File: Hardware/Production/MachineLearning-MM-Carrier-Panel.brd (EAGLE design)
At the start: 145 x 123.4 mm, 493 parts, among them J11 microSD, J15 CAMERA-HIMAX, J16 QWIIC_RIGHT_ANGLE, J17 USB-A, J18 JTAG, J19 MICROMOD-2222-C, J2 JTAG, J23 microSD, J28 CAMERA-HIMAX, J29 QWIIC_RIGHT_ANGLE, J3 QWIIC_RIGHT_ANGLE, J30 USB-A, J31 JTAG, J32 MICROMOD-2222-C, J36 microSD, J4 USB-A, J41 CAMERA-HIMAX, J42 QWIIC_RIGHT_ANGLE, J43 USB-A, J44 JTAG, J45 MICROMOD-2222-C, J49 microSD, J7 CAMERA-HIMAX, J9 MICROMOD-2222-C, U1 AP7361C-33FGE, U10 AP7361C-33FGE, U11 LIS2DH12, U12 AP2127K-1.8V, U2 LIS2DH12, U3 AP2127K-1.8V, U4 LIS2DH12, U5 AP7361C-33FGE, U6 AP2127K-1.8V, U7 AP7361C-33FGE, U8 LIS2DH12, U9 AP2127K-1.8V

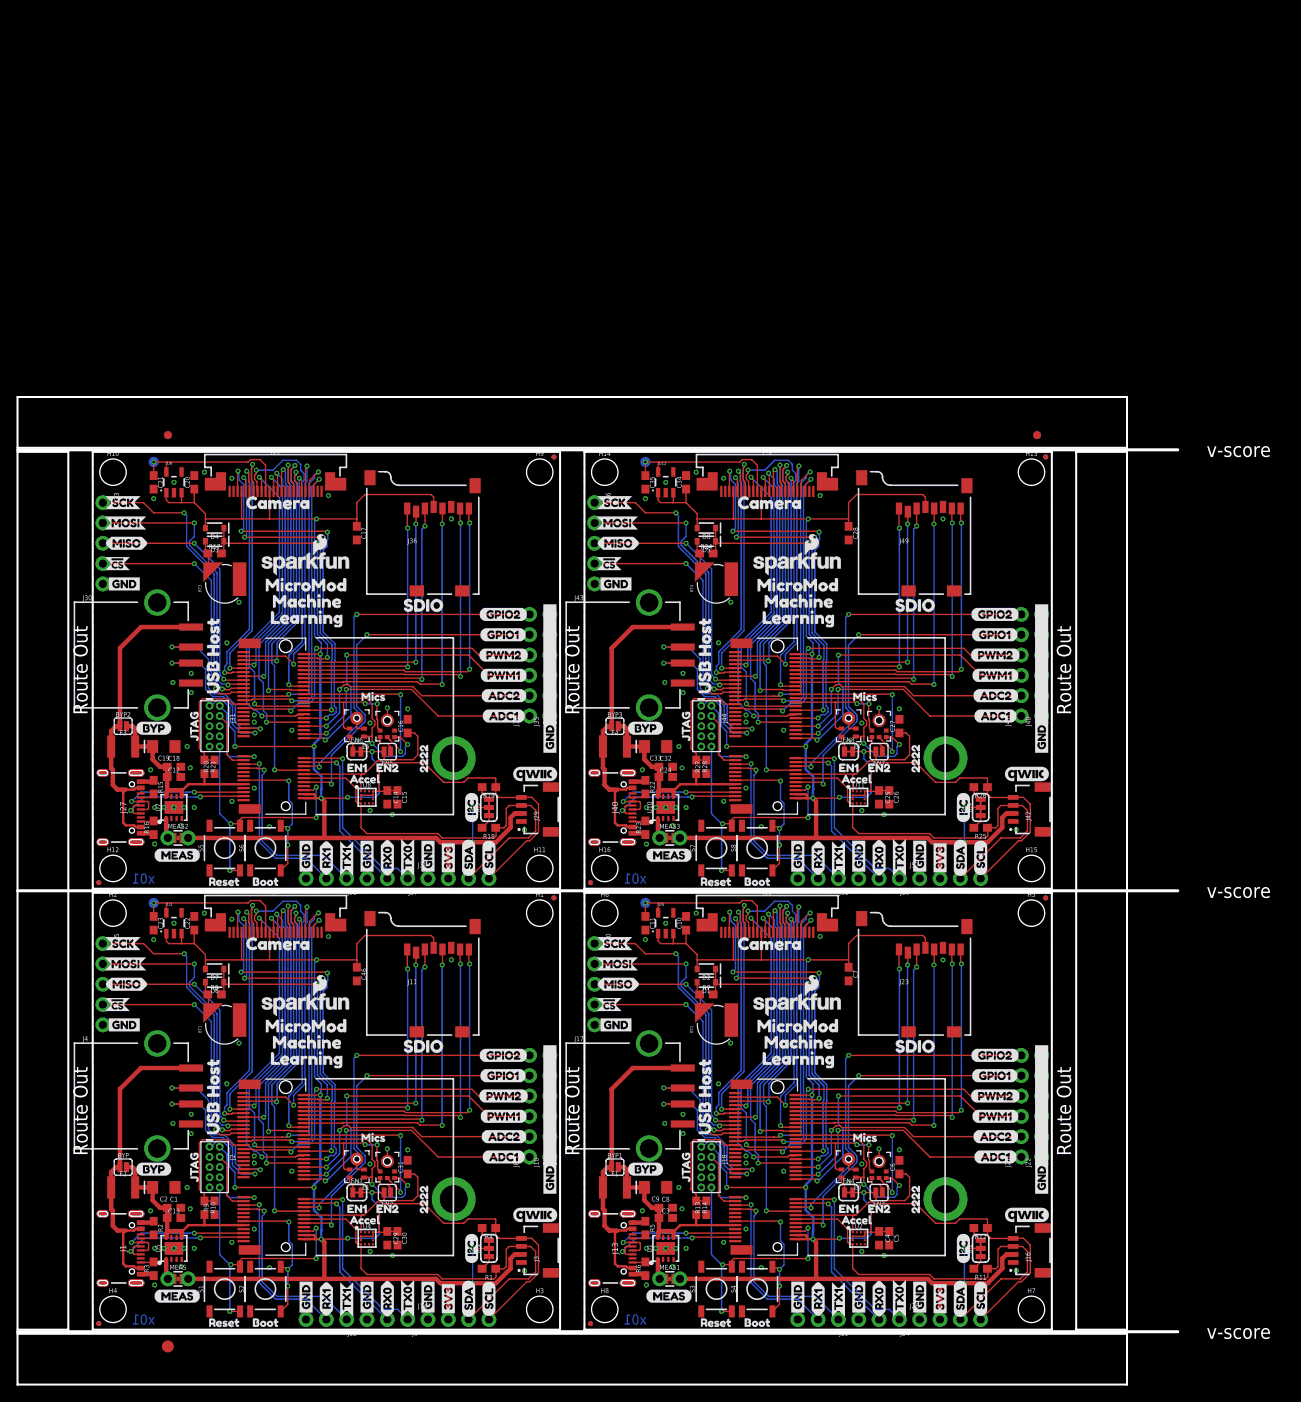
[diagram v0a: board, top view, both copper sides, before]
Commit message: Re-route camera connector for face up. Convert buzzard labels. Add power control to camera regulator.
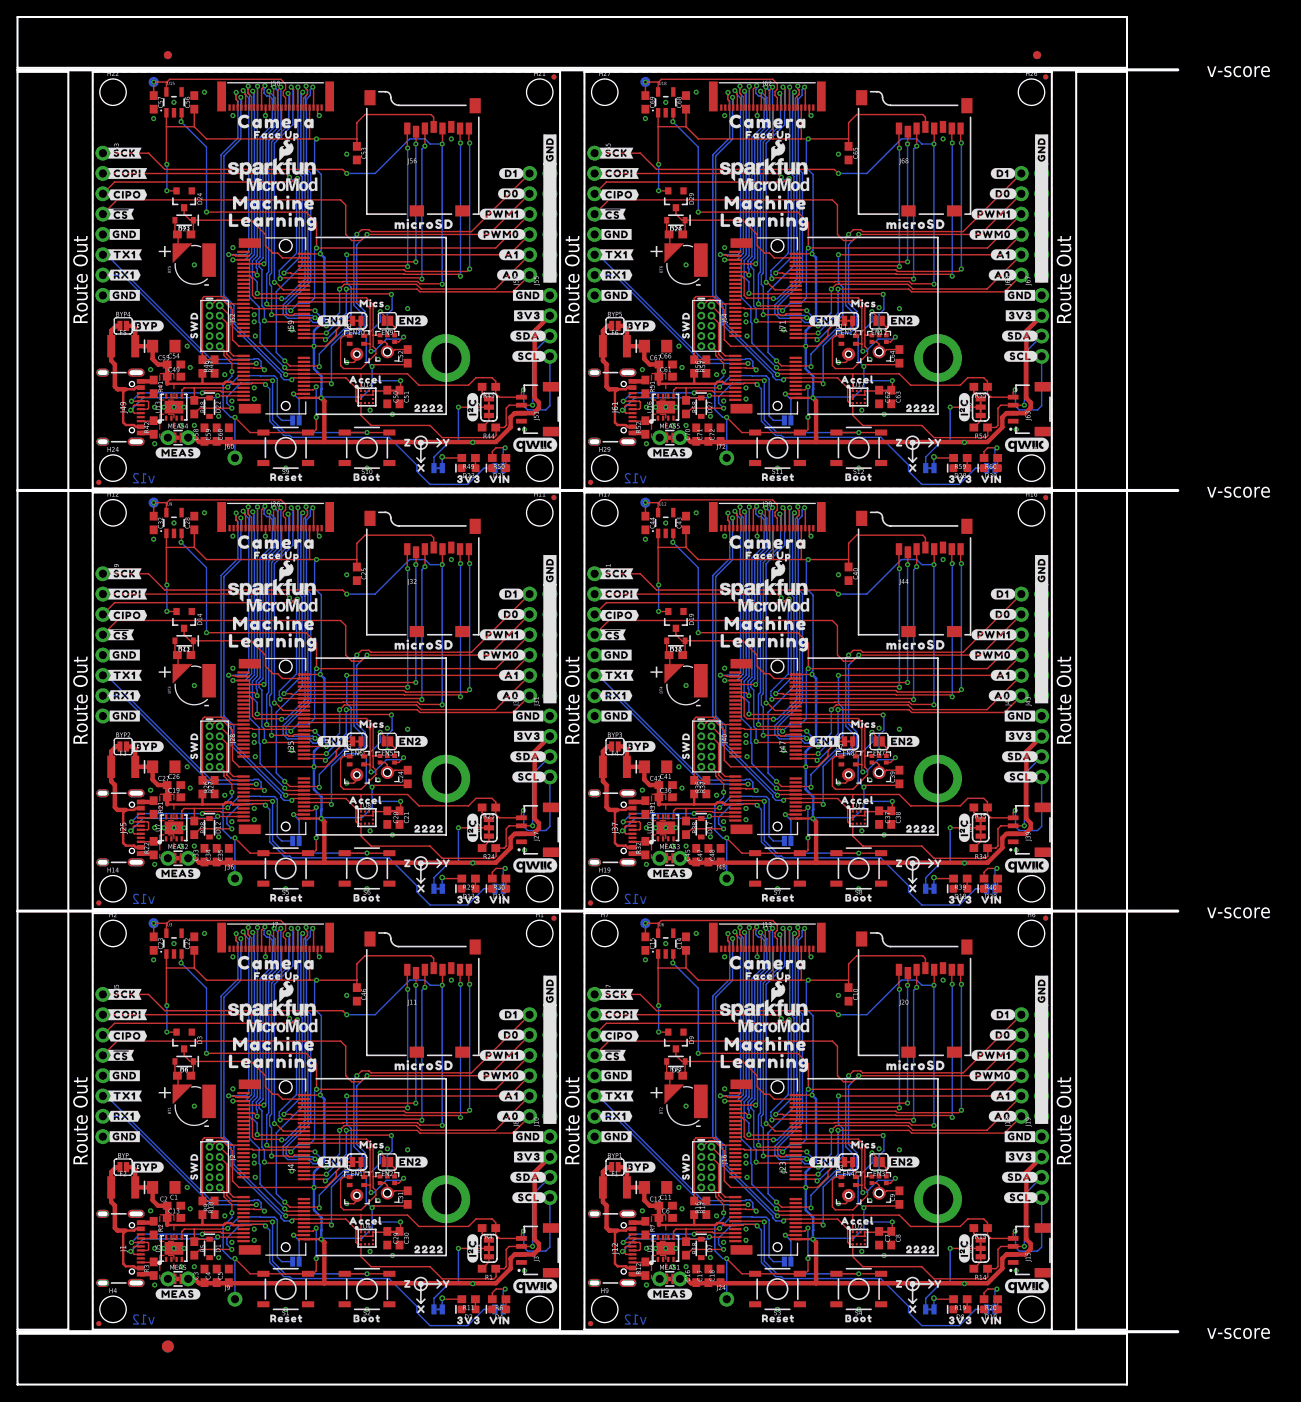
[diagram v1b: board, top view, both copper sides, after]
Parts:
- added 3V3_LED, 3V3_LED1, 3V3_LED2, 3V3_LED3, 3V3_LED4, 3V3_LED5, EN10, EN12, VIN_LED, VIN_LED1, VIN_LED2, VIN_LED3, VIN_LED4, VIN_LED5: (no value), SparkFun-Jumpers:SMT-JUMPER_2_NC_TRACE_SILK
- added BT5, BT6: ML414H, SparkFun-Batteries:ML414H_IV01E
- added BYP4, BYP5: JUMPER-SMT_2_NO_SILK, SparkFun-Jumpers:SMT-JUMPER_2_NO_SILK
- added C36, C48, C49, C60, C61, C72: 0.22uF, SparkFun-Capacitors:0603
- added C37, C43, C45, C50, C56, C58, C62, C68, C70: 1.0uF, SparkFun-Capacitors:0603
- added C38, C39, C40, C41, C44, C47, C51, C52, C53, C54, C57, C59, C63, C64, C65, C66, C69, C71: 0.1uF, SparkFun-Capacitors:0603
- added C42, C55, C67: 10uF, SparkFun-Capacitors:EIA3216
- added D10, D15, D20, D25, D30: Yellow, SparkFun-LED:LED-0603
- added D11, D16, D21, D26: 3A/10V/280mV, SparkFun-DiscreteSemi:SOD-323
- added D12, D17, D22, D27: 3.3V, SparkFun-DiscreteSemi:SOD-323
- added D13, D18, D23, D28: RED, SparkFun-LED:LED-0603
- added D14, D19, D24, D29, D9: BAS70-05, SparkFun-DiscreteSemi:SOT23-3
- added E$6: (no value), SparkFun-Retired:FIDUCIAL-1.5X3
- added E10, E12: ICS-43434, Teensy:ICS-43434
- added E11, E9: SPH0641LM4H-1, SparkFun-Sensors:SPH0641LM4H-1_MICROPHONE
- added EN11, EN9, VE, VE1, VE2, VE3, VE4, VE5: (no value), SparkFun-Jumpers:SMT-JUMPER_2_NO_SILK
- added F5, F6: 6V/2A, SparkFun-Fuses:1210
- added FD17, FD18, FD19, FD20, FD21, FD22, FD23, FD24: FIDUCIALUFIDUCIAL, SparkFun-Aesthetics:FIDUCIAL-MICRO
- added H17, H18, H19, H21, H22, H23, H24, H26, H27, H28, H29: STAND-OFF, SparkFun-Hardware:STAND-OFF
- added H20, H25, H30: STAND-OFF-REFLOW2.5MM_TALL, SparkFun-Hardware:STAND-OFF-REFLOW-M2.5
- added J53, J65: SPI, SparkFun-Connectors:1X05_NO_SILK
- added J54, J66: Dedicated, SparkFun-Connectors:1X06_NO_SILK
- added J55, J67: (no value), SparkFun-Connectors:1X06_NO_SILK
- added J56, J68: microSD, SparkFun-Connectors:MICRO-SD-SOCKET
- added J57, J69: UART, SparkFun-Connectors:1X03_NO_SILK
- added J58, J70: (no value), SparkFun-Connectors:1X04_NO_SILK
- added J59, J71: MICROMOD-2222-C, SparkFun-MicroMod:M.2-CONNECTOR-E
- added J60, J72: (no value), SparkFun-Connectors:1X01_NO_SILK
- added J61: (no value), SparkFun-Connectors:USB-C-16P-2LAYER-PADS
- added J62: CAMERA-HIMAXFACEUP, SparkFun-Connectors:FPC05024-42201
- added J63: QWIIC_RIGHT_ANGLE, SparkFun-Connectors:JST04_1MM_RA
- added J64: JTAG, SparkFun-Connectors:2X5-PTH-1.27MM
- added JP5, JP6: (no value), SparkFun-Jumpers:SMT-JUMPER_3_2-NC_TRACE_SILK
- added LOGO17, LOGO20, LOGO21, LOGO24: SFE_LOGO_NAME_FLAME.1_INCH, SparkFun-Aesthetics:SFE_LOGO_NAME_FLAME_.1
- added LOGO18, LOGO22: QWIIC_LOGO_CONNECTOR, SparkFun-Aesthetics:QWIIC_5.5MM
- added LOGO19, LOGO23: OSHW-LOGOMINI, SparkFun-Aesthetics:OSHW-LOGO-MINI
- added MEAS4, MEAS5: (no value), SparkFun-Jumpers:COMBO-JUMPER_2_NC_TRACE
- added R29, R39, R49, R59: 1k, SparkFun-Resistors:0603
- added R30, R40, R50, R60: 4.7k, SparkFun-Resistors:0603
- added R31, R32, R41, R42, R51, R52: 5.1k, SparkFun-Resistors:0603
- added R33, R43, R53: 3.3k, SparkFun-Resistors:0603
- added R34, R35, R44, R45, R54, R55: 2.2k, SparkFun-Resistors:0603
- added R36, R46, R56: 10k, SparkFun-Resistors:0603
- added R37, R47, R57: 20k, SparkFun-Resistors:0603
- added R38, R48, R58: 100k, SparkFun-Resistors:0603
- added S10, S12: BOOT, SparkFun-Switches:TACTILE_SWITCH_SMD_5.2MM
- added S11, S9: Reset, SparkFun-Switches:TACTILE_SWITCH_SMD_5.2MM
- added TP4, TP5: TEST-POINT3X5, SparkFun-Connectors:PAD.03X.05
- added U$257, U$324, U$391: (no value), output:#RST#1
- added U$258, U$325, U$392: (no value), output:#VE#0
- added U$259, U$326, U$393: (no value), output:#I�C#0
- added U$260, U$268, U$327, U$335, U$394, U$402: (no value), output:MACHINE0
- added U$261, U$267, U$328, U$334, U$395, U$401: (no value), output:LEARNING1
- added U$262, U$329, U$396: (no value), output:CAMERA0
- added U$263, U$330, U$397: (no value), output:FACE_UP0
- added U$264, U$331, U$398: (no value), output:#3V3#0
- added U$265, U$332, U$399: (no value), output:#VIN#1
- added U$266, U$333, U$400: (no value), output:MICROSD0
- added U$269, U$270, U$336, U$337: (no value), SparkFun-MicroMod:MICROMOD_LOGO_.35
- added U$271, U$272, U$338, U$339: (no value), output:##CS##3
- added U$273, U$274, U$340, U$341: (no value), output:#CIPO#2
- added U$275, U$276, U$342, U$343: (no value), output:#COPI#1
- added U$277, U$278, U$285, U$286, U$344, U$345, U$352, U$353: (no value), output:#GND#4
- added U$279, U$280, U$346, U$347: (no value), output:#RX1#6
- added U$281, U$282, U$348, U$349: (no value), output:#SCK#0
- added U$283, U$284, U$350, U$351: (no value), output:#TX1#5
- added U$287, U$288, U$354, U$355: (no value), output:#A0#5
- added U$289, U$290, U$356, U$357: (no value), output:#A1#4
- added U$291, U$292, U$358, U$359: (no value), output:#D0#1
- added U$293, U$294, U$360, U$361: (no value), output:#D1#0
- added U$295, U$296, U$362, U$363: (no value), output:#PWM0#3
- added U$297, U$298, U$364, U$365: (no value), output:#PWM1#2
- added U$299, U$300, U$303, U$304, U$366, U$367, U$370, U$371: (no value), output:#GND#0
- added U$301, U$302, U$368, U$369: (no value), output:#3V3#1
- added U$305, U$306, U$372, U$373: (no value), output:#SCL#3
- added U$307, U$308, U$374, U$375: (no value), output:#SDA#2
- added U$309, U$376: (no value), output:3V37
- added U$310, U$377: (no value), output:22223
- added U$311, U$378: (no value), output:ACCEL4
- added U$312, U$379: (no value), output:BOOT5
- added U$313, U$380: (no value), output:RESET6
- added U$314, U$381: (no value), output:VIN8
- added U$315, U$382: (no value), output:X1
- added U$316, U$383: (no value), output:Y2
- added U$317, U$384: (no value), output:Z0
- added U$318, U$385: (no value), output:#EN1#3
- added U$319, U$386: (no value), output:#EN2#4
- added U$320, U$387: (no value), output:#MEAS#2
- added U$321, U$388: (no value), output:SWD0
- added U$322, U$389: (no value), output:#BYP#1
- added U$323, U$390: (no value), output:MICS0
- added U13, U16: AP7361C-33FGE, SparkFun-IC-Power:UDFN-8
- added U14, U17: LIS2DH12, SparkFun-Sensors:LGA-12-LISDH12
- added U15, U18: AP2127K-1.8V, SparkFun-IC-Power:SOT23-5
- C10, C25, C34, C4: value 1.0uF -> 0.1uF
- C12: value 0.22uF -> 10uF; device SparkFun-Capacitors:0603 -> SparkFun-Capacitors:EIA3216
- C16, C28, C7: value 0.1uF -> 1.0uF
- C18, C35, C5, C6: value 0.1uF -> 0.22uF
- C19: value 10uF -> 0.22uF; device SparkFun-Capacitors:EIA3216 -> SparkFun-Capacitors:0603
- C24: value 0.22uF -> 0.1uF
- C27: value 0.1uF -> 10uF; device SparkFun-Capacitors:0603 -> SparkFun-Capacitors:EIA3216
- C3: value 0.22uF -> 1.0uF
- C33: value 10uF -> 1.0uF; device SparkFun-Capacitors:EIA3216 -> SparkFun-Capacitors:0603
- C9: value 10uF -> 0.1uF; device SparkFun-Capacitors:EIA3216 -> SparkFun-Capacitors:0603
- D1: value 3A/10V/280mV -> 3.3V
- D2, D8: value 1A/23V/620mV -> RED; device SparkFun-DiscreteSemi:SOD-323 -> SparkFun-LED:LED-0603
- D3: value 3A/10V/280mV -> BAS70-05; device SparkFun-DiscreteSemi:SOD-323 -> SparkFun-DiscreteSemi:SOT23-3
- D4: value 1A/23V/620mV -> Yellow; device SparkFun-DiscreteSemi:SOD-323 -> SparkFun-LED:LED-0603
- D7: value 1A/23V/620mV -> 3.3V
- F1, F2, F3, F4: value 2A/5V -> 6V/2A
- H10, H15, H5: value STAND-OFF -> STAND-OFF-REFLOW2.5MM_TALL; device SparkFun-Hardware:STAND-OFF -> SparkFun-Hardware:STAND-OFF-REFLOW-M2.5
- J1: device SparkFun-Connectors:USB-C-16P -> SparkFun-Connectors:USB-C-16P-2LAYER-PADS
- J12, J25, J37: device SparkFun-Connectors:1X03_NO_SILK -> SparkFun-Connectors:USB-C-16P-2LAYER-PADS
- J13: value (none) -> CAMERA-HIMAXFACEUP; device SparkFun-Connectors:USB-C-16P -> SparkFun-Connectors:FPC05024-42201
- J15: value CAMERA-HIMAX -> QWIIC_RIGHT_ANGLE; device SparkFun-Connectors:FPC-24-AMPHENOL-SFV24R-1STE1HLF -> SparkFun-Connectors:JST04_1MM_RA
- J16: value QWIIC_RIGHT_ANGLE -> JTAG; device SparkFun-Connectors:JST04_1MM_RA -> SparkFun-Connectors:2X5-PTH-1.27MM
- J17: value USB-A -> SPI; device SparkFun-Connectors:USB-A-S-SILK-FEMALE -> SparkFun-Connectors:1X05_NO_SILK
- J18: value JTAG -> Dedicated; device SparkFun-Connectors:2X5-PTH-1.27MM -> SparkFun-Connectors:1X06_NO_SILK
- J19: value MICROMOD-2222-C -> (none); device Teensy:M.2-CONNECTOR-E -> SparkFun-Connectors:1X06_NO_SILK
- J20: value (none) -> microSD; device SparkFun-Connectors:1X05_NO_SILK -> SparkFun-Connectors:MICRO-SD-SOCKET
- J21: value (none) -> UART; device SparkFun-Connectors:1X06_NO_SILK -> SparkFun-Connectors:1X03_NO_SILK
- J22, J34: device SparkFun-Connectors:1X06_NO_SILK -> SparkFun-Connectors:1X04_NO_SILK
- J23: value microSD -> MICROMOD-2222-C; device SparkFun-Connectors:MICRO-SD-SOCKET -> SparkFun-MicroMod:M.2-CONNECTOR-E
- J24: device SparkFun-Connectors:1X03_NO_SILK -> SparkFun-Connectors:1X01_NO_SILK
- J26: value (none) -> CAMERA-HIMAXFACEUP; device SparkFun-Connectors:1X04_NO_SILK -> SparkFun-Connectors:FPC05024-42201
- J27: value (none) -> QWIIC_RIGHT_ANGLE; device SparkFun-Connectors:USB-C-16P -> SparkFun-Connectors:JST04_1MM_RA
- J28: value CAMERA-HIMAX -> JTAG; device SparkFun-Connectors:FPC-24-AMPHENOL-SFV24R-1STE1HLF -> SparkFun-Connectors:2X5-PTH-1.27MM
- J29: value QWIIC_RIGHT_ANGLE -> SPI; device SparkFun-Connectors:JST04_1MM_RA -> SparkFun-Connectors:1X05_NO_SILK
- J30: value USB-A -> Dedicated; device SparkFun-Connectors:USB-A-S-SILK-FEMALE -> SparkFun-Connectors:1X06_NO_SILK
- J31: value JTAG -> (none); device SparkFun-Connectors:2X5-PTH-1.27MM -> SparkFun-Connectors:1X06_NO_SILK
- J32: value MICROMOD-2222-C -> microSD; device Teensy:M.2-CONNECTOR-E -> SparkFun-Connectors:MICRO-SD-SOCKET
- J33: value (none) -> UART; device SparkFun-Connectors:1X05_NO_SILK -> SparkFun-Connectors:1X03_NO_SILK
- J35, J47: value (none) -> MICROMOD-2222-C; device SparkFun-Connectors:1X06_NO_SILK -> SparkFun-MicroMod:M.2-CONNECTOR-E
- J36: value microSD -> (none); device SparkFun-Connectors:MICRO-SD-SOCKET -> SparkFun-Connectors:1X01_NO_SILK
- J38, J50: value (none) -> CAMERA-HIMAXFACEUP; device SparkFun-Connectors:1X03_NO_SILK -> SparkFun-Connectors:FPC05024-42201
- J39: value (none) -> QWIIC_RIGHT_ANGLE; device SparkFun-Connectors:1X04_NO_SILK -> SparkFun-Connectors:JST04_1MM_RA
- J4: value USB-A -> MICROMOD-2222-C; device SparkFun-Connectors:USB-A-S-SILK-FEMALE -> SparkFun-MicroMod:M.2-CONNECTOR-E
- J40: value (none) -> JTAG; device SparkFun-Connectors:USB-C-16P -> SparkFun-Connectors:2X5-PTH-1.27MM
- J41: value CAMERA-HIMAX -> SPI; device SparkFun-Connectors:FPC-24-AMPHENOL-SFV24R-1STE1HLF -> SparkFun-Connectors:1X05_NO_SILK
- J42: value QWIIC_RIGHT_ANGLE -> Dedicated; device SparkFun-Connectors:JST04_1MM_RA -> SparkFun-Connectors:1X06_NO_SILK
- J43: value USB-A -> (none); device SparkFun-Connectors:USB-A-S-SILK-FEMALE -> SparkFun-Connectors:1X06_NO_SILK
- J44: value JTAG -> microSD; device SparkFun-Connectors:2X5-PTH-1.27MM -> SparkFun-Connectors:MICRO-SD-SOCKET
- J45: value MICROMOD-2222-C -> UART; device Teensy:M.2-CONNECTOR-E -> SparkFun-Connectors:1X03_NO_SILK
- J46: device SparkFun-Connectors:1X05_NO_SILK -> SparkFun-Connectors:1X04_NO_SILK
- J48: device SparkFun-Connectors:1X06_NO_SILK -> SparkFun-Connectors:1X01_NO_SILK
- J49: value microSD -> (none); device SparkFun-Connectors:MICRO-SD-SOCKET -> SparkFun-Connectors:USB-C-16P-2LAYER-PADS
- J5: value (none) -> SPI
- J51: value (none) -> QWIIC_RIGHT_ANGLE; device SparkFun-Connectors:1X03_NO_SILK -> SparkFun-Connectors:JST04_1MM_RA
- J52: value (none) -> JTAG; device SparkFun-Connectors:1X04_NO_SILK -> SparkFun-Connectors:2X5-PTH-1.27MM
- J6: value (none) -> UART
- J7: value CAMERA-HIMAX -> CAMERA-HIMAXFACEUP; device SparkFun-Connectors:FPC-24-AMPHENOL-SFV24R-1STE1HLF -> SparkFun-Connectors:FPC05024-42201
- J8: value (none) -> Dedicated
- J9: value MICROMOD-2222-C -> (none); device Teensy:M.2-CONNECTOR-E -> SparkFun-Connectors:1X01_NO_SILK
- R11, R19: value 2.2k -> 1k
- R12: value 2.2k -> 5.1k
- R13: value 10k -> 3.3k
- R14: value 20k -> 2.2k
- R15: value 5.1k -> 2.2k
- R16: value 5.1k -> 10k
- R17: value 1k -> 20k
- R18: value 2.2k -> 100k
- R20: value 10k -> 4.7k
- R21: value 20k -> 5.1k
- R23: value 5.1k -> 3.3k
- R24: value 1k -> 2.2k
- R26: value 2.2k -> 10k
- R27: value 10k -> 20k
- R28: value 20k -> 100k
- R5: value 5.1k -> 100k
- R6: value 5.1k -> 4.7k
- R7: value 1k -> 5.1k
- R8: value 1k -> 3.3k
- U$1: device buzzard_labels (11):ACCEL6 -> output:#EN1#3
- U$10: device SparkFun-Buzzard:!CS_O -> output:#D0#1
- U$100, U$167: device SparkFun-Buzzard:GND_P -> output:#3V3#1
- U$101: device buzzard_labels (6):RX01 -> output:#3V3#1
- U$102, U$166: device buzzard_labels (6):TX02 -> output:#GND#0
- U$103, U$11: device SparkFun-Buzzard:GND_P -> output:#GND#0
- U$104: device SparkFun-Buzzard:3V3_P -> output:#SCL#3
- U$105: device SparkFun-Buzzard:SDA_IO -> output:#SCL#3
- U$106: device SparkFun-Buzzard:SCL_IO -> output:#SDA#2
- U$107: device SparkFun-Buzzard:SCK_O -> output:#SDA#2
- U$108: device SparkFun-Buzzard:MOSI_O -> output:3V37
- U$109: device SparkFun-Buzzard:MISO_I -> output:22223
- U$110: device SparkFun-Buzzard:!CS_O -> output:ACCEL4
- U$111: device SparkFun-Buzzard:GND_P -> output:BOOT5
- U$112: device buzzard_labels (9):22229 -> output:RESET6
- U$113: device buzzard_labels (9):GPIO110 -> output:VIN8
- U$114: device buzzard_labels (9):GPIO211 -> output:X1
- U$115: device buzzard_labels (10):ADC12 -> output:Y2
- U$116: device buzzard_labels (10):ADC23 -> output:Z0
- U$117: device buzzard_labels (10):PWM10 -> output:#EN1#3
- U$118, U$185: device buzzard_labels (10):PWM21 -> output:#EN2#4
- U$119: device buzzard_labels (9):GPIO211 -> output:#MEAS#2
- U$12: device buzzard_labels (9):GPIO110 -> output:#GND#0
- U$120: device buzzard_labels (9):GPIO110 -> output:SWD0
- U$121: device buzzard_labels (10):PWM21 -> output:#BYP#1
- U$122: device buzzard_labels (10):PWM10 -> output:MICS0
- U$123, U$17: device buzzard_labels (10):ADC23 -> output:#RST#1
- U$124: device buzzard_labels (10):ADC12 -> output:#VE#0
- U$125: device buzzard_labels (11):MICROMOD0 -> output:#I�C#0
- U$126: device buzzard_labels (11):MACHINE2 -> output:MACHINE0
- U$127: device buzzard_labels (11):LEARNING3 -> output:LEARNING1
- U$128: device SparkFun-Buzzard:GND_P -> output:CAMERA0
- U$129: device buzzard_labels (9):RESET3 -> output:FACE_UP0
- U$13: device buzzard_labels (9):GPIO211 -> output:#3V3#1
- U$130: device SparkFun-Buzzard:MEAS -> output:#3V3#0
- U$131: device SparkFun-Buzzard:MOSI_O -> output:#VIN#1
- U$132: device SparkFun-Buzzard:MISO_I -> output:MICROSD0
- U$133: device SparkFun-Buzzard:SCK_O -> output:LEARNING1
- U$134: device SparkFun-Buzzard:!CS_O -> output:MACHINE0
- U$135, U$136, U$53, U$54: device SparkFun-Buzzard:GND_P -> SparkFun-MicroMod:MICROMOD_LOGO_.35
- U$137: device SparkFun-Buzzard:JTAG_TO -> output:##CS##3
- U$138: device buzzard_labels (10):BOOT2 -> output:##CS##3
- U$139: device buzzard_labels (10):USB_HOST0 -> output:#CIPO#2
- U$14: device buzzard_labels (10):PWM10 -> output:#3V3#1
- U$140: device buzzard_labels (10):SDIO1 -> output:#CIPO#2
- U$141: device buzzard_labels (11):ACCEL6 -> output:#COPI#1
- U$142: device buzzard_labels (11):CAMERA5 -> output:#COPI#1
- U$143: device buzzard_labels (11):LEARNING3 -> output:#GND#4
- U$144: device buzzard_labels (11):MACHINE2 -> output:#GND#4
- U$145, U$64: device buzzard_labels (11):MICROMOD0 -> output:#RX1#6
- U$146: device buzzard_labels (12):MICS0 -> output:#RX1#6
- U$147: device SparkFun-Buzzard:BYP -> output:#SCK#0
- U$148: device buzzard_labels (6):RX01 -> output:#SCK#0
- U$149: device buzzard_labels (6):RX10 -> output:#TX1#5
- U$15: device buzzard_labels (10):PWM21 -> output:#GND#0
- U$150: device buzzard_labels (6):TX02 -> output:#TX1#5
- U$151: device buzzard_labels (6):TX13 -> output:#GND#4
- U$152: device SparkFun-Buzzard:GND_P -> output:#GND#4
- U$153, U$221, U$6: device SparkFun-Buzzard:GND_P -> output:#A0#5
- U$154: device buzzard_labels (7):EN13 -> output:#A0#5
- U$155: device buzzard_labels (7):EN24 -> output:#A1#4
- U$156: device SparkFun-Buzzard:I2C -> output:#A1#4
- U$157, U$225: device SparkFun-Buzzard:GND_P -> output:#D0#1
- U$158: device SparkFun-Buzzard:3V3_P -> output:#D0#1
- U$159: device SparkFun-Buzzard:SDA_IO -> output:#D1#0
- U$16: device buzzard_labels (10):ADC12 -> output:#GND#0
- U$160: device SparkFun-Buzzard:SCL_IO -> output:#D1#0
- U$161, U$228, U$32: device SparkFun-Buzzard:GND_P -> output:#PWM0#3
- U$162: device buzzard_labels (6):RX10 -> output:#PWM0#3
- U$163: device buzzard_labels (6):TX13 -> output:#PWM1#2
- U$164, U$231, U$42, U$97: device SparkFun-Buzzard:GND_P -> output:#PWM1#2
- U$165: device buzzard_labels (6):RX01 -> output:#GND#0
- U$168: device SparkFun-Buzzard:3V3_P -> output:#3V3#1
- U$169, U$233: device SparkFun-Buzzard:SDA_IO -> output:#GND#0
- U$170: device SparkFun-Buzzard:SCL_IO -> output:#GND#0
- U$171: device SparkFun-Buzzard:SCK_O -> output:#SCL#3
- U$172: device SparkFun-Buzzard:MOSI_O -> output:#SCL#3
- U$173, U$51: device SparkFun-Buzzard:MISO_I -> output:#SDA#2
- U$174: device SparkFun-Buzzard:!CS_O -> output:#SDA#2
- U$175, U$36: device SparkFun-Buzzard:GND_P -> output:3V37
- U$176: device buzzard_labels (9):22229 -> output:22223
- U$177: device buzzard_labels (9):GPIO110 -> output:ACCEL4
- U$178: device buzzard_labels (9):GPIO211 -> output:BOOT5
- U$179: device buzzard_labels (10):ADC12 -> output:RESET6
- U$18: device SparkFun-Buzzard:JTAG_TO -> output:#VE#0
- U$180: device buzzard_labels (10):ADC23 -> output:VIN8
- U$181: device buzzard_labels (10):PWM10 -> output:X1
- U$182, U$249: device buzzard_labels (10):PWM21 -> output:Y2
- U$183: device buzzard_labels (9):GPIO211 -> output:Z0
- U$184: device buzzard_labels (9):GPIO110 -> output:#EN1#3
- U$186: device buzzard_labels (10):PWM10 -> output:#MEAS#2
- U$187: device buzzard_labels (10):ADC23 -> output:SWD0
- U$188: device buzzard_labels (10):ADC12 -> output:#BYP#1
- U$189: device buzzard_labels (11):MICROMOD0 -> output:MICS0
- U$19: device buzzard_labels (10):BOOT2 -> output:#MEAS#2
- U$190: device buzzard_labels (11):MACHINE2 -> output:#RST#1
- U$191: device buzzard_labels (11):LEARNING3 -> output:#VE#0
- U$192, U$23: device SparkFun-Buzzard:GND_P -> output:#I�C#0
- U$193: device buzzard_labels (9):RESET3 -> output:MACHINE0
- U$194: device SparkFun-Buzzard:MEAS -> output:LEARNING1
- U$195: device SparkFun-Buzzard:MOSI_O -> output:CAMERA0
- U$196: device SparkFun-Buzzard:MISO_I -> output:FACE_UP0
- U$197: device SparkFun-Buzzard:SCK_O -> output:#3V3#0
- U$198: device SparkFun-Buzzard:!CS_O -> output:#VIN#1
- U$199: device SparkFun-Buzzard:GND_P -> output:MICROSD0
- U$2: device buzzard_labels (9):RESET3 -> output:#EN2#4
- U$20: device buzzard_labels (10):USB_HOST0 -> output:#VIN#1
- U$200: device SparkFun-Buzzard:GND_P -> output:LEARNING1
- U$201: device SparkFun-Buzzard:JTAG_TO -> output:MACHINE0
- U$202: device buzzard_labels (10):BOOT2 -> SparkFun-MicroMod:MICROMOD_LOGO_.35
- U$203: device buzzard_labels (10):USB_HOST0 -> SparkFun-MicroMod:MICROMOD_LOGO_.35
- U$204: device buzzard_labels (10):SDIO1 -> output:##CS##3
- U$205: device buzzard_labels (11):ACCEL6 -> output:##CS##3
- U$206: device buzzard_labels (11):CAMERA5 -> output:#CIPO#2
- U$207: device buzzard_labels (11):LEARNING3 -> output:#CIPO#2
- U$208: device buzzard_labels (11):MACHINE2 -> output:#COPI#1
- U$209: device buzzard_labels (11):MICROMOD0 -> output:#COPI#1
- U$21: device buzzard_labels (10):SDIO1 -> output:SWD0
- U$210, U$82: device buzzard_labels (12):MICS0 -> output:#GND#4
- U$211: device SparkFun-Buzzard:BYP -> output:#GND#4
- U$212: device buzzard_labels (6):RX01 -> output:#RX1#6
- U$213: device buzzard_labels (6):RX10 -> output:#RX1#6
- U$214: device buzzard_labels (6):TX02 -> output:#SCK#0
- U$215: device buzzard_labels (6):TX13 -> output:#SCK#0
- U$216, U$217: device SparkFun-Buzzard:GND_P -> output:#TX1#5
- U$218: device buzzard_labels (7):EN13 -> output:#GND#4
- U$219: device buzzard_labels (7):EN24 -> output:#GND#4
- U$22: device buzzard_labels (11):MACHINE2 -> output:FACE_UP0
- U$220: device SparkFun-Buzzard:I2C -> output:#A0#5
- U$222: device SparkFun-Buzzard:3V3_P -> output:#A1#4
- U$223: device SparkFun-Buzzard:SDA_IO -> output:#A1#4
- U$224: device SparkFun-Buzzard:SCL_IO -> output:#D0#1
- U$226, U$29: device buzzard_labels (6):RX10 -> output:#D1#0
- U$227, U$31: device buzzard_labels (6):TX13 -> output:#D1#0
- U$229: device buzzard_labels (6):RX01 -> output:#PWM0#3
- U$230: device buzzard_labels (6):TX02 -> output:#PWM1#2
- U$232: device SparkFun-Buzzard:3V3_P -> output:#GND#0
- U$234: device SparkFun-Buzzard:SCL_IO -> output:#3V3#1
- U$235: device SparkFun-Buzzard:SCK_O -> output:#3V3#1
- U$236: device SparkFun-Buzzard:MOSI_O -> output:#GND#0
- U$237: device SparkFun-Buzzard:MISO_I -> output:#GND#0
- U$238: device SparkFun-Buzzard:!CS_O -> output:#SCL#3
- U$239: device SparkFun-Buzzard:GND_P -> output:#SCL#3
- U$24: device buzzard_labels (11):MICROMOD0 -> SparkFun-MicroMod:MICROMOD_LOGO_.35
- U$240: device buzzard_labels (9):22229 -> output:#SDA#2
- U$241: device buzzard_labels (9):GPIO110 -> output:#SDA#2
- U$242: device buzzard_labels (9):GPIO211 -> output:3V37
- U$243: device buzzard_labels (10):ADC12 -> output:22223
- U$244: device buzzard_labels (10):ADC23 -> output:ACCEL4
- U$245: device buzzard_labels (10):PWM10 -> output:BOOT5
- U$246: device buzzard_labels (10):PWM21 -> output:RESET6
- U$247: device buzzard_labels (9):GPIO211 -> output:VIN8
- U$248: device buzzard_labels (9):GPIO110 -> output:X1
- U$25: device buzzard_labels (6):RX10 -> output:#D0#1
- U$250: device buzzard_labels (10):PWM10 -> output:Z0
- U$251: device buzzard_labels (10):ADC23 -> output:#EN1#3
- U$252: device buzzard_labels (10):ADC12 -> output:#EN2#4
- U$253: device buzzard_labels (11):MICROMOD0 -> output:#MEAS#2
- U$254: device buzzard_labels (11):MACHINE2 -> output:SWD0
- U$255: device buzzard_labels (11):LEARNING3 -> output:#BYP#1
- U$256: device SparkFun-Buzzard:GND_P -> output:MICS0
- U$26: device buzzard_labels (12):MICS0 -> output:MACHINE0
- U$27: device SparkFun-Buzzard:BYP -> output:LEARNING1
- U$28: device buzzard_labels (6):RX01 -> output:MICROSD0
- U$3: device buzzard_labels (11):CAMERA5 -> output:CAMERA0
- U$30: device buzzard_labels (6):TX02 -> output:LEARNING1
- U$33: device SparkFun-Buzzard:GND_P -> output:#BYP#1
- U$34: device buzzard_labels (7):EN13 -> SparkFun-MicroMod:MICROMOD_LOGO_.35
- U$35: device buzzard_labels (7):EN24 -> output:##CS##3
- U$37: device SparkFun-Buzzard:I2C -> output:MACHINE0
- U$38: device SparkFun-Buzzard:3V3_P -> output:22223
- U$39: device SparkFun-Buzzard:SDA_IO -> output:ACCEL4
- U$4: device buzzard_labels (11):LEARNING3 -> output:#3V3#0
- U$40: device SparkFun-Buzzard:SCL_IO -> output:BOOT5
- U$41: device buzzard_labels (6):TX13 -> output:#PWM0#3
- U$43: device buzzard_labels (6):RX01 -> output:#SCL#3
- U$44: device buzzard_labels (6):TX02 -> output:#SCL#3
- U$45: device SparkFun-Buzzard:GND_P -> output:RESET6
- U$46: device SparkFun-Buzzard:3V3_P -> output:VIN8
- U$47: device SparkFun-Buzzard:SDA_IO -> output:X1
- U$48: device SparkFun-Buzzard:SCL_IO -> output:Y2
- U$49: device SparkFun-Buzzard:SCK_O -> output:#PWM1#2
- U$5: device SparkFun-Buzzard:MEAS -> output:MICS0
- U$50: device SparkFun-Buzzard:MOSI_O -> output:#SDA#2
- U$52: device SparkFun-Buzzard:!CS_O -> output:Z0
- U$55: device buzzard_labels (9):22229 -> output:##CS##3
- U$56: device buzzard_labels (9):RESET3 -> output:##CS##3
- U$57: device SparkFun-Buzzard:MEAS -> output:#CIPO#2
- U$58: device buzzard_labels (9):GPIO211 -> output:#CIPO#2
- U$59: device buzzard_labels (9):GPIO110 -> output:#COPI#1
- U$60: device buzzard_labels (10):PWM21 -> output:#COPI#1
- U$61: device buzzard_labels (10):PWM10 -> output:#GND#4
- U$62: device buzzard_labels (10):ADC23 -> output:#GND#4
- U$63: device buzzard_labels (10):ADC12 -> output:#RX1#6
- U$65: device buzzard_labels (11):MACHINE2 -> output:#SCK#0
- U$66: device buzzard_labels (11):LEARNING3 -> output:#SCK#0
- U$67: device SparkFun-Buzzard:MOSI_O -> output:#TX1#5
- U$68: device SparkFun-Buzzard:MISO_I -> output:##CS##3
- U$69: device SparkFun-Buzzard:SCK_O -> output:#CIPO#2
- U$7: device SparkFun-Buzzard:MOSI_O -> output:#A0#5
- U$70: device SparkFun-Buzzard:!CS_O -> output:#CIPO#2
- U$71, U$72: device SparkFun-Buzzard:GND_P -> output:#COPI#1
- U$73: device SparkFun-Buzzard:JTAG_TO -> output:#GND#4
- U$74: device buzzard_labels (10):BOOT2 -> output:#GND#4
- U$75: device buzzard_labels (10):USB_HOST0 -> output:#RX1#6
- U$76: device buzzard_labels (10):SDIO1 -> output:#RX1#6
- U$77: device buzzard_labels (11):ACCEL6 -> output:#SCK#0
- U$78: device buzzard_labels (11):CAMERA5 -> output:#SCK#0
- U$79: device buzzard_labels (11):LEARNING3 -> output:#TX1#5
- U$8: device SparkFun-Buzzard:MISO_I -> output:#A1#4
- U$80: device buzzard_labels (11):MACHINE2 -> output:#TX1#5
- U$81: device buzzard_labels (11):MICROMOD0 -> output:#GND#4
- U$83: device SparkFun-Buzzard:BYP -> output:#TX1#5
- U$84: device buzzard_labels (6):RX01 -> output:#GND#4
- U$85: device buzzard_labels (6):RX10 -> output:#GND#4
- U$86: device buzzard_labels (6):TX02 -> output:#A0#5
- U$87: device buzzard_labels (6):TX13 -> output:#A0#5
- U$88, U$89: device SparkFun-Buzzard:GND_P -> output:#A1#4
- U$9: device SparkFun-Buzzard:SCK_O -> output:#A1#4
- U$90: device buzzard_labels (7):EN13 -> output:#D0#1
- U$91: device buzzard_labels (7):EN24 -> output:#D0#1
- U$92: device SparkFun-Buzzard:I2C -> output:#D1#0
- U$93: device SparkFun-Buzzard:GND_P -> output:#D1#0
- U$94: device SparkFun-Buzzard:3V3_P -> output:#PWM0#3
- U$95: device SparkFun-Buzzard:SDA_IO -> output:#PWM0#3
- U$96: device SparkFun-Buzzard:SCL_IO -> output:#PWM1#2
- U$98: device buzzard_labels (6):RX10 -> output:#GND#0
- U$99: device buzzard_labels (6):TX13 -> output:#GND#0
- U1, U10, U5, U7: device ublox:8-UDFN -> SparkFun-IC-Power:UDFN-8
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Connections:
- net N$1 renamed VREG_3.3V
- net N$13 renamed VREG_3.3V1
- net N$22 renamed VREG_3.3V2
- net N$30 renamed VREG_3.3V3
- removed net ADC_1ST: J8.1, J9.34
- removed net ADC_1ST1: J19.34, J21.1
- removed net ADC_1ST2: J32.34, J34.1
- removed net ADC_1ST3: J45.34, J47.1
- removed net ADC_2ND: J8.2, J9.38
- removed net ADC_2ND1: J19.38, J21.2
- removed net ADC_2ND2: J32.38, J34.2
- removed net ADC_2ND3: J45.38, J47.2
- removed net CAMERA_I2C_SCL: J7.21, J9.53
- removed net CAMERA_I2C_SCL1: J15.21, J19.53
- removed net CAMERA_I2C_SCL2: J28.21, J32.53
- removed net CAMERA_I2C_SCL3: J41.21, J45.53
- removed net CAMERA_I2C_SDA: J7.22, J9.51
- removed net CAMERA_I2C_SDA1: J15.22, J19.51
- removed net CAMERA_I2C_SDA2: J28.22, J32.51
- removed net CAMERA_I2C_SDA3: J41.22, J45.51
- removed net CAMERA_PCLK: J7.17, J9.56
- removed net CAMERA_PCLK1: J15.17, J19.56
- removed net CAMERA_PCLK2: J28.17, J32.56
- removed net CAMERA_PCLK3: J41.17, J45.56
- removed net CAMERA_TRIG: J7.7, J9.67
- removed net CAMERA_TRIG1: J15.7, J19.67
- removed net CAMERA_TRIG2: J28.7, J32.67
- removed net CAMERA_TRIG3: J41.7, J45.67
- removed net GPIO_1ST: J8.5, J9.10
- removed net GPIO_1ST1: J19.10, J21.5
- removed net GPIO_1ST2: J32.10, J34.5
- removed net GPIO_1ST3: J45.10, J47.5
- removed net GPIO_2ND: J8.6, J9.18
- removed net GPIO_2ND1: J19.18, J21.6
- removed net GPIO_2ND2: J32.18, J34.6
- removed net GPIO_2ND3: J45.18, J47.6
- removed net I2S_SD: E2.6, J9.54
- removed net I2S_SD1: E4.6, J19.54
- removed net I2S_SD2: E6.6, J32.54
- removed net I2S_SD3: E8.6, J45.54
- removed net N$18 (its old number): J27.B5, R16.2
- removed net N$19 (its old number): BT3.+, D3.A, R17.1
- removed net PWM_1ST: J8.3, J9.32
- removed net PWM_1ST1: J19.32, J21.3
- removed net PWM_1ST2: J32.32, J34.3
- removed net PWM_1ST3: J45.32, J47.3
- removed net PWM_2ND: J8.4, J9.47
- removed net PWM_2ND1: J19.47, J21.4
- removed net PWM_2ND2: J32.47, J34.4
- removed net PWM_2ND3: J45.47, J47.4
- removed net RX0: J6.2, J9.20
- removed net RX7: J45.19, J51.2
- removed net SD_CLK: J11.SCLK, J9.60
- removed net SD_CLK1: J19.60, J23.SCLK
- removed net SD_CLK2: J32.60, J36.SCLK
- removed net SD_CLK3: J45.60, J49.SCLK
- removed net SD_CMD: J11.DI, J9.62
- removed net SD_CMD1: J19.62, J23.DI
- removed net SD_CMD2: J32.62, J36.DI
- removed net SD_CMD3: J45.62, J49.DI
- removed net SD_DAT0: J11.DO, J9.64
- removed net SD_DAT1: J11.RSV2, J9.66
- removed net SD_DAT10: J32.70, J36.CS
- removed net SD_DAT11: J32.68, J36.RSV1
- removed net SD_DAT12: J45.66, J49.RSV2
- removed net SD_DAT13: J45.64, J49.DO
- removed net SD_DAT14: J45.70, J49.CS
- removed net SD_DAT15: J45.68, J49.RSV1
- removed net SD_DAT2: J11.RSV1, J9.68
- removed net SD_DAT3: J11.CS, J9.70
- removed net SD_DAT4: J19.66, J23.RSV2
- removed net SD_DAT5: J19.64, J23.DO
- removed net SD_DAT6: J19.70, J23.CS
- removed net SD_DAT7: J19.68, J23.RSV1
- removed net SD_DAT8: J32.66, J36.RSV2
- removed net SD_DAT9: J32.64, J36.DO
- removed net SPI_!CS!: J5.4, J9.55
- removed net SPI_!CS!1: J19.55, J20.4
- removed net SPI_!CS!2: J32.55, J33.4
- removed net SPI_!CS!3: J45.55, J46.4
- removed net SPI_CLK: J5.1, J9.57
- removed net SPI_CLK1: J19.57, J20.1
- removed net SPI_CLK2: J32.57, J33.1
- removed net SPI_CLK3: J45.57, J46.1
- removed net SPI_MISO: J5.3, J9.61
- removed net SPI_MISO1: J19.61, J20.3
- removed net SPI_MISO2: J32.61, J33.3
- removed net SPI_MISO3: J45.61, J46.3
- removed net SPI_MOSI: J5.2, J9.59
- removed net SPI_MOSI1: J19.59, J20.2
- removed net SPI_MOSI2: J32.59, J33.2
- removed net SPI_MOSI3: J45.59, J46.2
- removed net TX0: J6.1, J9.22
- removed net TX7: J45.17, J51.1
- removed net USBHOST_D+: J4.D+, J9.35
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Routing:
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- added copper zone on layer 1, net GND4
- added copper zone on layer 16, net GND4
- added copper zone on layer 1, net GND5
- added copper zone on layer 16, net GND5
- added copper zone on layer 1, net VIN
- added copper zone on layer 1, net VIN1
- added copper zone on layer 1, net VIN2
- added copper zone on layer 1, net VIN3
- added copper zone on layer 1, net VIN4
- added copper zone on layer 1, net VIN5
- added copper zone on layer 1, net VREG_3.3V
- added copper zone on layer 1, net VREG_3.3V1
- added copper zone on layer 1, net VREG_3.3V2
- added copper zone on layer 1, net VREG_3.3V3
- added copper zone on layer 1, net VREG_3.3V4
- added copper zone on layer 1, net VREG_3.3V5
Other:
- board size 145 x 123.4 mm -> 145 x 170.9 mm
- board text added: "+"
- board text added: "-"
- board text added: "v12"
- board text removed: "x01"

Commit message: Update production files to v13
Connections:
- removed net SDIO_DAT1: J11.DAT1, J4.66
- removed net SDIO_DAT10: J56.DAT2, J59.68
- removed net SDIO_DAT11: J68.DAT1, J71.66
- removed net SDIO_DAT12: J68.DAT2, J71.68
- removed net SDIO_DAT2: J11.DAT2, J4.68
- removed net SDIO_DAT3: J20.DAT1, J23.66
- removed net SDIO_DAT4: J20.DAT2, J23.68
- removed net SDIO_DAT5: J32.DAT1, J35.66
- removed net SDIO_DAT6: J32.DAT2, J35.68
- removed net SDIO_DAT7: J44.DAT1, J47.66
- removed net SDIO_DAT8: J44.DAT2, J47.68
- removed net SDIO_DAT9: J56.DAT1, J59.66
- removed net SPI_!CS!/SDIO_DAT1: J20.CS/DAT3, J23.70
- removed net SPI_!CS!/SDIO_DAT2: J32.CS/DAT3, J35.70
- removed net SPI_!CS!/SDIO_DAT3: J11.CS/DAT3, J4.70
- removed net SPI_!CS!/SDIO_DAT4: J44.CS/DAT3, J47.70
- removed net SPI_!CS!/SDIO_DAT5: J56.CS/DAT3, J59.70
- removed net SPI_!CS!/SDIO_DAT6: J68.CS/DAT3, J71.70
- removed net SPI_SDI: J11.DO/DAT0, J4.64, J5.3
- removed net SPI_SDI1: J17.3, J20.DO/DAT0, J23.64
- removed net SPI_SDI2: J29.3, J32.DO/DAT0, J35.64
- removed net SPI_SDI3: J41.3, J44.DO/DAT0, J47.64
- removed net SPI_SDI4: J53.3, J56.DO/DAT0, J59.64
- removed net SPI_SDI5: J65.3, J68.DO/DAT0, J71.64
- removed net SPI_SDO: J11.DI/CMD, J4.62, J5.2
- removed net SPI_SDO1: J17.2, J20.DI/CMD, J23.62
- removed net SPI_SDO2: J29.2, J32.DI/CMD, J35.62
- removed net SPI_SDO3: J41.2, J44.DI/CMD, J47.62
- removed net SPI_SDO4: J53.2, J56.DI/CMD, J59.62
- removed net SPI_SDO5: J65.2, J68.DI/CMD, J71.62
- new net SPI_!CS!: J11.CS/DAT3, J4.55
- new net SPI_!CS!1: J20.CS/DAT3, J23.55
- new net SPI_!CS!2: J32.CS/DAT3, J35.55
- new net SPI_!CS!3: J44.CS/DAT3, J47.55
- new net SPI_!CS!4: J56.CS/DAT3, J59.55
- new net SPI_!CS!5: J68.CS/DAT3, J71.55
- new net SPI_CIPO: J11.DO/DAT0, J4.61, J5.3
- new net SPI_CIPO1: J17.3, J20.DO/DAT0, J23.61
- new net SPI_CIPO2: J29.3, J32.DO/DAT0, J35.61
- new net SPI_CIPO3: J41.3, J44.DO/DAT0, J47.61
- new net SPI_CIPO4: J53.3, J56.DO/DAT0, J59.61
- new net SPI_CIPO5: J65.3, J68.DO/DAT0, J71.61
- new net SPI_COPI: J11.DI/CMD, J4.59, J5.2
- new net SPI_COPI1: J17.2, J20.DI/CMD, J23.59
- new net SPI_COPI2: J29.2, J32.DI/CMD, J35.59
- new net SPI_COPI3: J41.2, J44.DI/CMD, J47.59
- new net SPI_COPI4: J53.2, J56.DI/CMD, J59.59
- new net SPI_COPI5: J65.2, J68.DI/CMD, J71.59
- net SPI_SCK: now also J4.57; no longer J4.60
- net SPI_SCK1: now also J23.57; no longer J23.60
- net SPI_SCK2: now also J35.57; no longer J35.60
- net SPI_SCK3: now also J47.57; no longer J47.60
- net SPI_SCK4: now also J59.57; no longer J59.60
- net SPI_SCK5: now also J71.57; no longer J71.60
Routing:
- net SPI_SDI2: track 78.5 -> 0.00 mm, vias 4 -> 0
- net SPI_SDI: track 78.5 -> 0.00 mm, vias 4 -> 0
- net SPI_SDI3: track 78.5 -> 0.00 mm, vias 4 -> 0
- net SPI_SDI1: track 78.5 -> 0.00 mm, vias 4 -> 0
- net SPI_SDI5: track 78.5 -> 0.00 mm, vias 4 -> 0
- net SPI_SDI4: track 78.5 -> 0.00 mm, vias 4 -> 0
- net SPI_SDO4: track 74.3 -> 0.00 mm, vias 4 -> 0
- net SPI_SDO: track 74.3 -> 0.00 mm, vias 4 -> 0
- net SPI_SDO2: track 74.3 -> 0.00 mm, vias 4 -> 0
- net SPI_SDO5: track 74.3 -> 0.00 mm, vias 4 -> 0
- net SPI_SDO3: track 74.3 -> 0.00 mm, vias 4 -> 0
- net SPI_SDO1: track 74.3 -> 0.00 mm, vias 4 -> 0
- net SPI_CIPO5: track 0.00 -> 69.0 mm, vias 0 -> 2
- net SPI_CIPO4: track 0.00 -> 69.0 mm, vias 0 -> 2
- net SPI_CIPO3: track 0.00 -> 69.0 mm, vias 0 -> 2
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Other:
- board text added: "v13"
- board text removed: "v12"
